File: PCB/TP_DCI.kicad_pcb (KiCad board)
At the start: 2 copper layers, 55 parts, among them K1 G5V-2-5DC, K2 G5V-2-5DC, P1 Conn_02x20, P2 Conn_02x20, Q1 BC817W, Q2 BC817W, U1 PS2805-4, U2 ACS725xLCTR-10AU, U4 ACS725xLCTR-10AU, U5 24AA1025, U6 DS3231

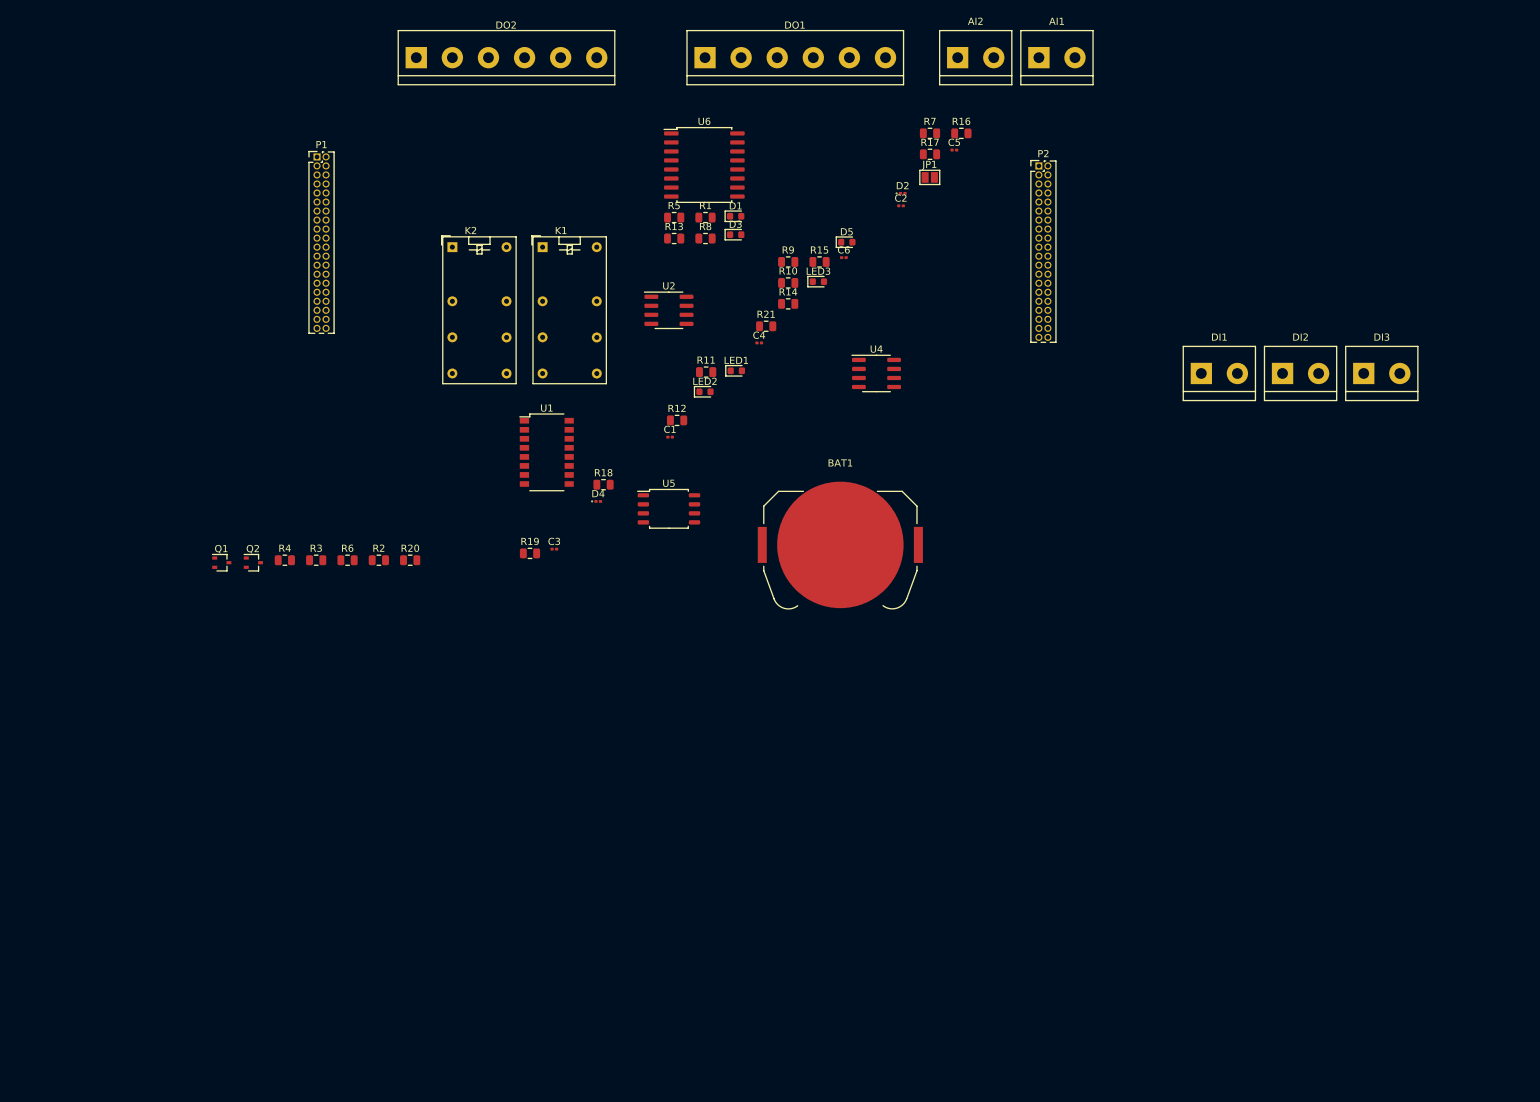
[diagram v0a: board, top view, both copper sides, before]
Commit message: Se incorpora plantilla de poncho EDU-CIAA
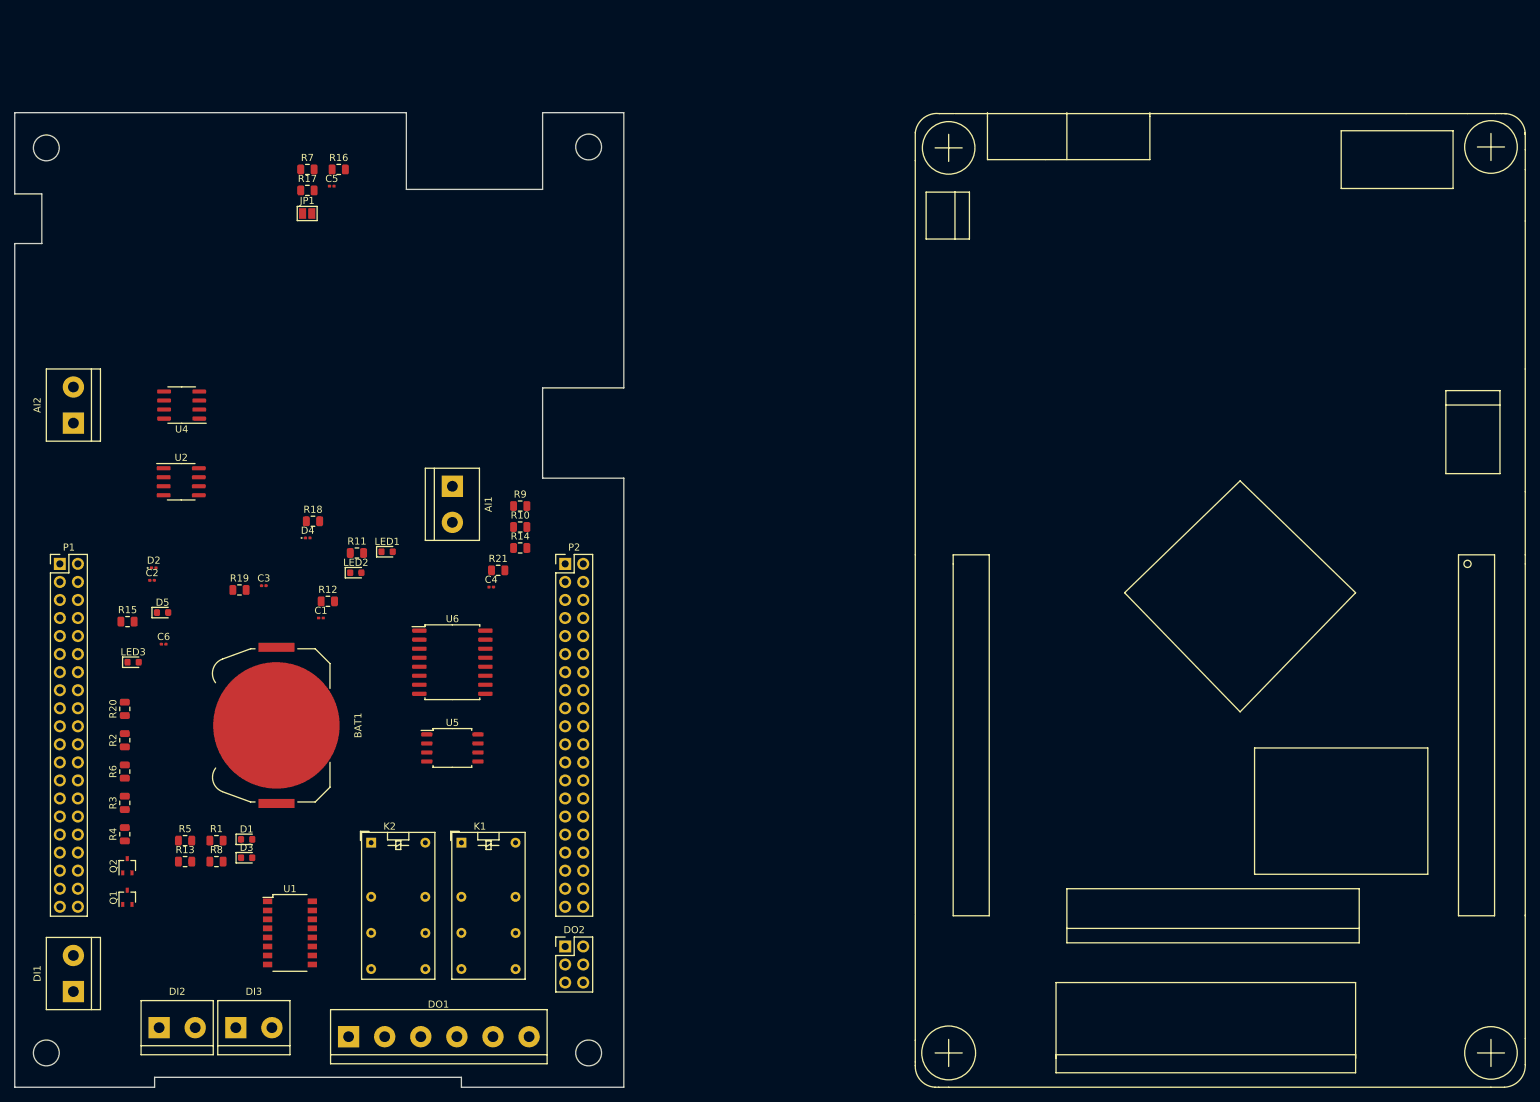
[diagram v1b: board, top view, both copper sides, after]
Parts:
- added MP1: Plantilla_EDU-CIAA, Poncho_Esqueleto:Plantilla_EDU-CIAA, F.Cu at (249.6, 91.6)
- DO2: footprint TerminalBlock:TerminalBlock_bornier-6_P5.08mm -> Connector_PinHeader_2.54mm:PinHeader_2x03_P2.54mm_Vertical
- P1, P2: footprint Connector_PinHeader_1.27mm:PinHeader_2x20_P1.27mm_Vertical -> Connector_PinHeader_2.54mm:PinHeader_2x20_P2.54mm_Vertical
- moved DI3 183.5 mm to (76.2, 156.8)
- moved DI2 183.0 mm to (65.4, 156.8)
- moved DI1 181.0 mm to (53.3, 151.8), turned to 90 degrees
- moved DO1 146.6 mm to (92.1, 158.1)
- moved AI2 134.7 mm to (53.3, 71.8), turned to 90 degrees
- moved DO2 126.8 mm to (122.6, 145.4)
- moved D2 117.9 mm to (64.7, 92.1)
- moved C2 117.9 mm to (64.4, 93.9)
- moved D3 111.5 mm to (77.7, 132.9)
- moved D1 111.5 mm to (77.7, 130.3)
- moved R1 111.5 mm to (73.5, 130.5)
- moved R13 111.5 mm to (69.1, 133.5)
- moved R5 111.5 mm to (69.1, 130.5)
- moved R8 111.5 mm to (73.5, 133.5)
- moved LED3 110.3 mm to (61.7, 105.4)
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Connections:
- DO1 pad 4: /COM1B -> /COM2A
- DO1 pad 5: /NC1B -> /NC2A
- DO1 pad 6: /NA1B -> /NA2A
- DO2 pad 1: /COM2A -> /COM2B
- DO2 pad 2: /NC2A -> /NC2B
- DO2 pad 3: /NA2A -> /NA2B
- DO2 pad 4: /COM2B -> /COM1B
- DO2 pad 5: /NC2B -> /NC1B
- DO2 pad 6: /NA2B -> /NA1B
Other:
- board outline added: 85.7 x 137.2 mm

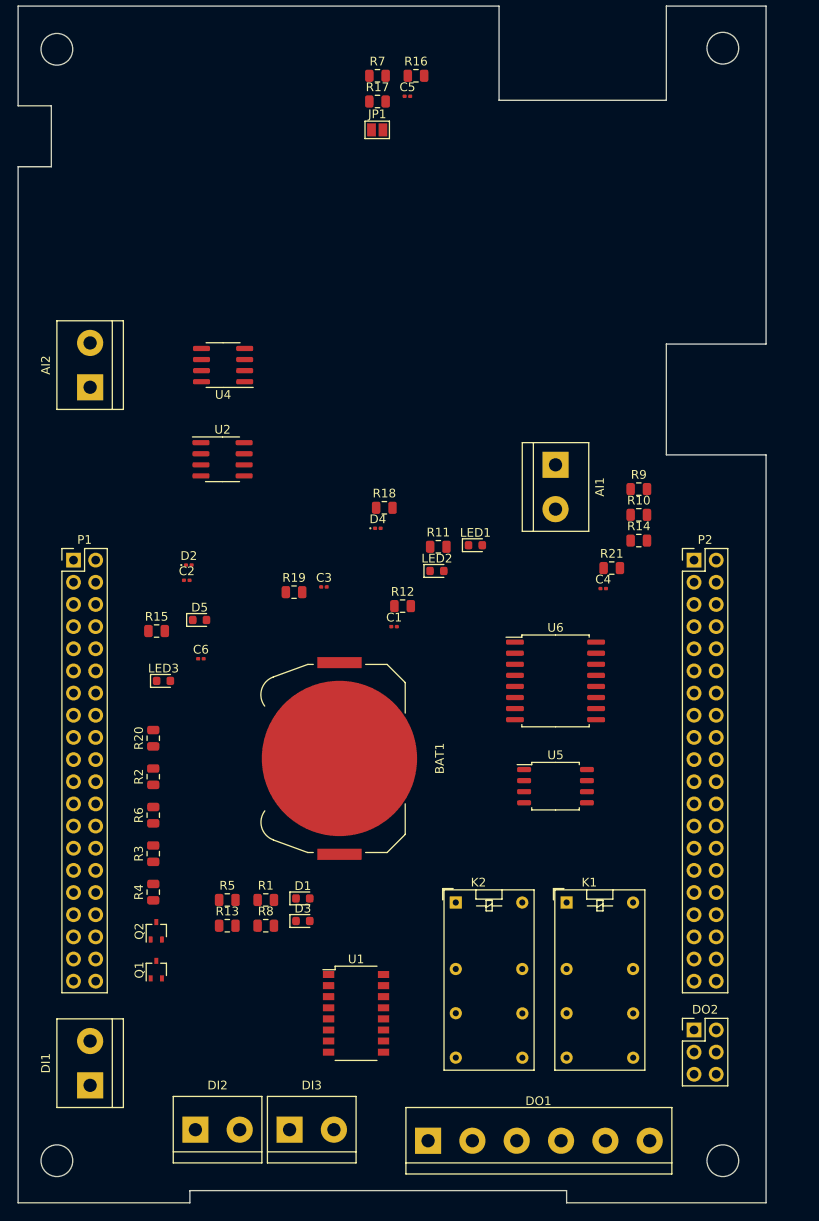
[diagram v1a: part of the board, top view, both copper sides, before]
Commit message: actualizacion de footprints y 3Dshapes
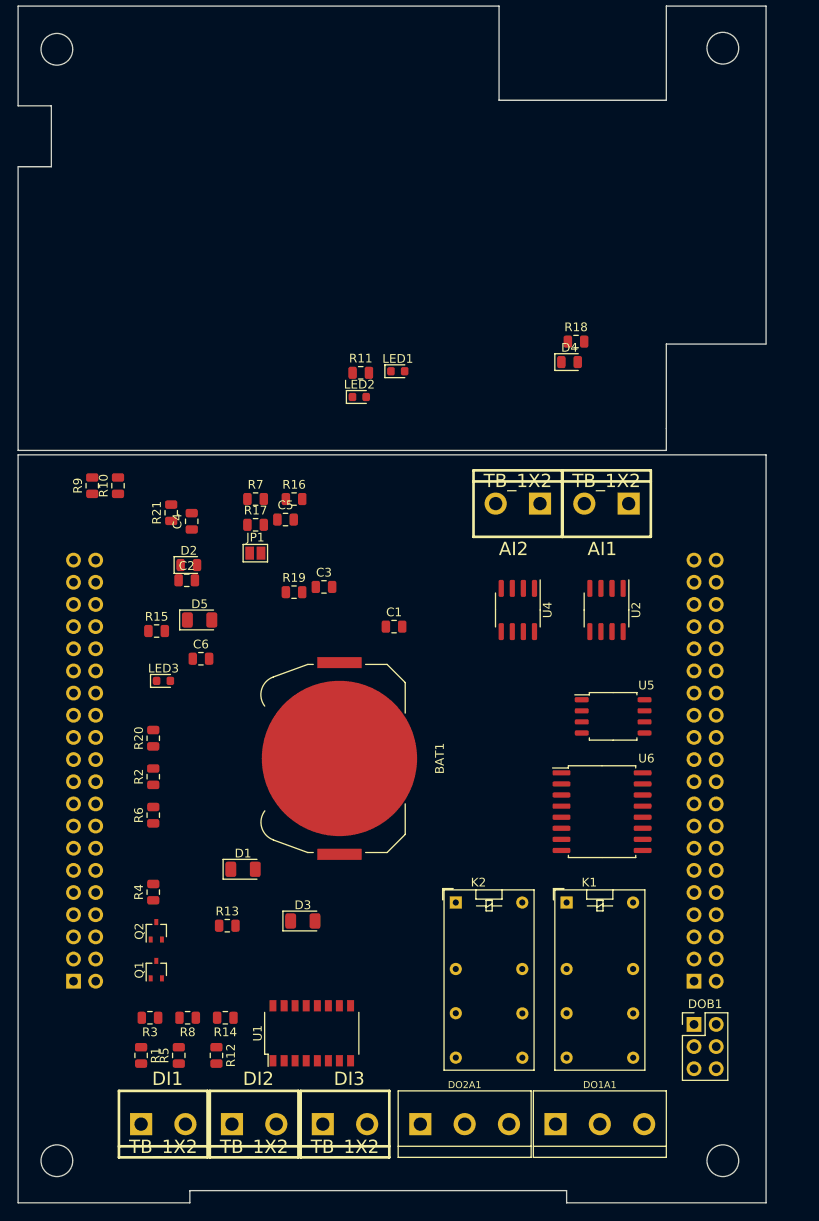
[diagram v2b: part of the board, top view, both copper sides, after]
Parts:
- removed DO1: 01x06, TerminalBlock:TerminalBlock_bornier-6_P5.08mm
- added DO1A1: TB_1X3, Libreria_EDU_CIAA_NXP:bornier3, F.Cu at (111.8, 156.2)
- added DO2A1: TB_1X3, Libreria_EDU_CIAA_NXP:bornier3, F.Cu at (96.3, 156.2)
- AI1, AI2, DI1, DI2, DI3: value 01x02 -> TB_1X2; footprint TerminalBlock:TerminalBlock_bornier-2_P5.08mm -> Libreria_EDU_CIAA_NXP:bornier2
- C1, C2, C3, C4, C5, C6: footprint Capacitor_SMD:C_0201_0603Metric -> Capacitor_SMD:C_0805_2012Metric
- D1, D3, D5: footprint Diode_SMD:D_0603_1608Metric -> Diode_SMD:D_1206_3216Metric
- D2, D4: footprint LED_SMD:LED_0201_0603Metric -> LED_SMD:LED_0805_2012Metric
- P1, P2: moved to B.Cu
- moved R14 72.4 mm to (68.8, 144.0), turned to 180 degrees
- moved R9 62.6 mm to (53.6, 83.0), turned to 90 degrees
- moved R10 59.8 mm to (56.5, 83.0), turned to 90 degrees
- moved R12 55.7 mm to (67.8, 148.3), turned to 270 degrees
- moved R21 50.9 mm to (62.6, 86.1), turned to 90 degrees
- moved AI2 50.8 mm to (102.4, 85.1), turned to 180 degrees
- moved JP1 50.5 mm to (72.3, 90.8)
- moved R16 50.5 mm to (76.7, 84.6)
- moved R17 50.5 mm to (72.3, 87.5)
- moved R7 50.5 mm to (72.3, 84.6)
- moved C5 50.5 mm to (75.7, 86.9)
- moved P1 48.3 mm to (51.4, 139.8)
- moved P2 48.3 mm to (122.6, 139.8)
- moved C4 47.8 mm to (65.0, 87.1), turned to 90 degrees
- moved U2 47.3 mm to (112.5, 97.3), turned to 270 degrees
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- renumbered DO2 to DOB1
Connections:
- DOB1 pad 4: /COM1B -> /COM2B
- DOB1 pad 5: /NC1B -> /NC2B
- DOB1 pad 6: /NA1B -> /NA2B
- K2 pad 11: /NC1B -> /NC2B
- K2 pad 13: /COM1B -> /COM2B
- K2 pad 4: /COM1A -> /COM2A
- K2 pad 6: /NC1A -> /NC2A
- K2 pad 8: /NA1A -> /NA2A
- K2 pad 9: /NA1B -> /NA2B
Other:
- outline, holes or cut-outs redrawn

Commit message: actualizacion de esquematico con nuevos componentes, se agregan vias termicas en PCB
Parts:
- removed AI1, AI2: TB_1X2, Libreria_EDU_CIAA_NXP:bornier2
- removed DOB1: 01x06, Connector_PinHeader_2.54mm:PinHeader_2x03_P2.54mm_Vertical
- removed MP1: Plantilla_EDU-CIAA, Poncho_Esqueleto:Plantilla_EDU-CIAA
- removed P2: Conn_02x20, Connector_PinHeader_2.54mm:PinHeader_2x20_P2.54mm_Vertical
- added AI1+1: TB_1X1, CIAA_footprints:wurth_connector, F.Cu at (77.8, 183.4)
- added AI1-1: TB_1X1, CIAA_footprints:wurth_connector, F.Cu at (77.9, 172.0)
- added AI2+1: TB_1X1, CIAA_footprints:wurth_connector, F.Cu at (44.1, 172.0)
- added AI2-1: TB_1X1, CIAA_footprints:wurth_connector, F.Cu at (44.1, 183.4)
- added F1: Fiducial, Fiducial:Fiducial_0.5mm_Mask1mm, F.Cu at (30.0, 20.4)
- added F2: Fiducial, Fiducial:Fiducial_0.5mm_Mask1mm, F.Cu at (101.1, 30.7)
- added F3: Fiducial, Fiducial:Fiducial_0.5mm_Mask1mm, F.Cu at (22.6, 144.3)
- added F4: Fiducial, Fiducial:Fiducial_0.5mm_Mask1mm, F.Cu at (95.0, 193.2)
- added H1: Hole, MountingHole:MountingHole_2.1mm, F.Cu at (24.1, 161.3)
- added H2: Hole, MountingHole:MountingHole_2.1mm, F.Cu at (100.5, 161.3)
- added H3: Hole, MountingHole:MountingHole_2.1mm, F.Cu at (24.1, 191.9)
- added H4: Hole, MountingHole:MountingHole_2.1mm, F.Cu at (100.3, 191.9)
- added H5: MountingHole, MountingHole:MountingHole_2.1mm, F.Cu at (24.1, 22.9)
- added H6: MountingHole, MountingHole:MountingHole_2.1mm, F.Cu at (100.5, 22.7)
- added H7: MountingHole, MountingHole:MountingHole_2.1mm, F.Cu at (24.1, 150.2)
- added H8: MountingHole, MountingHole:MountingHole_2.1mm, F.Cu at (100.5, 150.2)
- added J8: Molex_KK254, Connector_Molex:Molex_KK-254_AE-6410-04A_1x04_P2.54mm_Vertical, F.Cu at (64.8, 165.6)
- added J9: Molex_KK254, Connector_Molex:Molex_KK-254_AE-6410-04A_1x04_P2.54mm_Vertical, F.Cu at (57.1, 145.8)
- JP1: footprint Jumper:SolderJumper-2_P1.3mm_Open_Pad1.0x1.5mm -> Connector_PinHeader_2.54mm:PinHeader_1x02_P2.54mm_Vertical
- K1, K2: value G5V-2-5DC -> G5V-1; footprint Relay_THT:Relay_DPDT_Omron_G5V-2 -> Relay_THT:Relay_SPDT_Omron_G5V-1
- LED1, LED2, LED3: footprint LED_SMD:LED_0603_1608Metric -> LED_SMD:LED_0805_2012Metric
- P1: value Conn_02x20 -> Conn_Poncho2P_2x_20x2; footprint Connector_PinHeader_2.54mm:PinHeader_2x20_P2.54mm_Vertical -> Poncho_Esqueleto:Conn_Poncho_SinBorde; moved to F.Cu
- moved DO1 144.4 mm to (46.5, 27.4), turned to 180 degrees
- moved DO2 133.3 mm to (62.0, 27.4), turned to 180 degrees
- moved DI1 114.5 mm to (28.6, 46.6), turned to 270 degrees
- moved DI2 108.3 mm to (28.6, 57.0), turned to 270 degrees
- moved K2 106.0 mm to (43.8, 38.1)
- moved Q1 105.7 mm to (87.6, 36.2), turned to 0 degrees
- moved K1 104.5 mm to (59.7, 38.1)
- moved DI3 103.9 mm to (28.6, 67.4), turned to 270 degrees
- moved U2 92.9 mm to (66.0, 177.7), turned to 180 degrees
- moved U4 92.9 mm to (55.9, 177.7), turned to 0 degrees
- moved U1 92.2 mm to (45.7, 59.7), turned to 0 degrees
- moved D1 91.7 mm to (78.1, 35.6)
- moved R6 80.9 mm to (70.8, 40.6), turned to 0 degrees
- moved C1 78.4 mm to (62.9, 173.4), turned to 180 degrees
- moved C3 78.1 mm to (62.9, 170.8), turned to 180 degrees
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- renumbered DO1A1 to DO1, DO2A1 to DO2
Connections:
- C1 pad 1: VDDA -> Net-(C1-Pad1)
- C1 pad 2: GNDA -> Net-(C1-Pad2)
- C2 pad 1: VDDA -> Net-(C1-Pad1)
- C2 pad 2: GNDA -> Net-(C1-Pad2)
- C3 pad 2: GNDA -> Net-(C1-Pad2)
- C4 pad 1: +3V3 -> /+3.3V
- C5 pad 1: +3V3 -> /+3.3V
- C6 pad 2: GNDA -> Net-(C1-Pad2)
- DO1 pad 1: /COM1A -> /COM1
- DO1 pad 2: /NC1A -> /NC1
- DO1 pad 3: /NA1A -> /NA1
- DO2 pad 1: /COM2A -> /COM2
- DO2 pad 2: /NC2A -> /NC2
- DO2 pad 3: /NA2A -> /NA2
- JP1 pad 1: Net-(D5-Pad1) -> Net-(BAT1-Pad1)
- JP1 pad 2: Net-(BAT1-Pad1) -> Net-(D5-Pad1)
- K1 pad 1: +5V -> /NC1
- K1 pad 6: /NC1A -> /COM1
- K1 pad 9: /NA1B -> Net-(D1-Pad2)
- K2 pad 1: +5V -> /NC2
- K2 pad 6: /NC2A -> /COM2
- K2 pad 9: /NA2B -> Net-(D3-Pad2)
- P1 pad 10: Net-(P1-Pad10) -> (no net)
- P1 pad 11: Net-(P1-Pad11) -> /ADC_CH2
- P1 pad 12: Net-(P1-Pad12) -> GNDA
- P1 pad 13: Net-(P1-Pad13) -> /ADC_CH1
- P1 pad 14: Net-(P1-Pad14) -> GNDA
- P1 pad 15: Net-(P1-Pad15) -> (no net)
- P1 pad 16: Net-(P1-Pad16) -> (no net)
- P1 pad 17: GND -> VDDA
- P1 pad 18: Net-(P1-Pad18) -> (no net)
- P1 pad 19: GND -> /SDA
- P1 pad 20: Net-(P1-Pad20) -> (no net)
- P1 pad 21: Net-(P1-Pad21) -> /SCL
- P1 pad 22: Net-(P1-Pad22) -> (no net)
- P1 pad 23: Net-(P1-Pad23) -> (no net)
- P1 pad 24: Net-(P1-Pad24) -> (no net)
- P1 pad 25: Net-(P1-Pad25) -> (no net)
- P1 pad 26: Net-(P1-Pad26) -> (no net)
- P1 pad 27: Net-(P1-Pad27) -> (no net)
- P1 pad 28: Net-(P1-Pad28) -> GND
- P1 pad 29: /GPIO0 -> (no net)
- P1 pad 3: GND -> (no net)
- P1 pad 30: Net-(P1-Pad30) -> GND
- P1 pad 31: /GPIO2 -> (no net)
- P1 pad 32: /GPIO1 -> GND
- P1 pad 33: /GPIO4 -> (no net)
- P1 pad 34: /GPIO3 -> (no net)
- P1 pad 35: /GPIO6 -> (no net)
- P1 pad 36: /GPIO5 -> (no net)
- P1 pad 37: GND -> (no net)
- P1 pad 38: /GPIO7 -> (no net)
- P1 pad 39: GND -> (no net)
- P1 pad 4: Net-(P1-Pad4) -> GND
- P1 pad 40: /GPIO8 -> (no net)
- P1 pad 5: GND -> (no net)
- P1 pad 6: Net-(P1-Pad6) -> (no net)
- P1 pad 7: GND -> (no net)
- P1 pad 8: Net-(P1-Pad8) -> (no net)
- P1 pad 9: Net-(P1-Pad9) -> (no net)
- R18 pad 1: Net-(D5-Pad2) -> +3V3
- R18 pad 2: +3V3 -> Net-(D5-Pad2)
- U1 pad 10: Net-(U1-Pad10) -> (no net)
- U1 pad 7: Net-(U1-Pad7) -> (no net)
- U1 pad 8: Net-(U1-Pad8) -> (no net)
- U1 pad 9: Net-(U1-Pad9) -> (no net)
- U2 pad 5: GNDA -> Net-(C1-Pad2)
- U2 pad 7: /ADC_CH1 -> /ANALOG_1
- U2 pad 8: VDDA -> Net-(C1-Pad1)
- U4 pad 5: GNDA -> Net-(C1-Pad2)
- U4 pad 7: /ADC_CH2 -> /ANALOG_2
- U4 pad 8: VDDA -> Net-(C1-Pad1)
- U6 pad 1: Net-(U6-Pad1) -> (no net)
- U6 pad 4: Net-(U6-Pad4) -> (no net)
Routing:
- net Net-(C1-Pad1): track 0.00 -> 18.2 mm
- net /ANALOG_1: track 0.00 -> 14.0 mm
- net /ANALOG_2: track 0.00 -> 13.1 mm
- net Net-(C6-Pad1): track 0.00 -> 6.20 mm
- net Net-(C1-Pad2): track 0.00 -> 4.36 mm
- net Net-(AI2-1-Pad1): vias 0 -> 19
- net Net-(AI2+1-Pad1): vias 0 -> 19
- net Net-(AI1-1-Pad1): vias 0 -> 19
- net Net-(AI1+1-Pad1): vias 0 -> 19
- added copper zone on B.Cu, net Net-(AI1+1-Pad1)
- added copper zone on F.Cu, net Net-(AI1+1-Pad1)
- added copper zone on B.Cu, net Net-(AI1-1-Pad1)
- added copper zone on F.Cu, net Net-(AI1-1-Pad1)
- added copper zone on B.Cu, net Net-(AI2+1-Pad1)
- added copper zone on F.Cu, net Net-(AI2+1-Pad1)
- added copper zone on B.Cu, net Net-(AI2-1-Pad1)
- added copper zone on F.Cu, net Net-(AI2-1-Pad1)
- added copper zone on F.Cu, net Net-(C1-Pad2)
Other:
- board size 85.7 x 137.2 mm -> 85.7 x 178.9 mm
- board text added: "+"
- board text added: "+5V"
- board text added: "-"
- board text added: "COM NC NA"
- board text added: "EDU-CIAA PONCHO FOTOVOLTAICO"
- board text added: "ENTRADAS DIGITALES"
- board text added: "GND"
- board text added: "RESET"
- board text added: "SALIDAS DIGITALES"
